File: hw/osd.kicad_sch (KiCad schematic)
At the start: 60 parts, among them U801 SN74CBTLV3125RGYR, U802 SN74CBTLV3125RGYR, U803 XLV320ADC5140IRTWR, U804 SN74CBTLV3125RGYR, U805 SN74CBTLV3125RGYR

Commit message: Now two CPLDs, new placement for better routing of clocks and symmetry for delay. Not routed yet but placement is "complete".
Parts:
- added R806, R807: 22, Resistor_SMD:R_0402_1005Metric, symbol Device:R_Small_US
- C817, C818, C830, C831, C836, C837, C842, C843: footprint Capacitor_SMD:C_0603_1608Metric -> Capacitor_SMD:C_0402_1005Metric
- U801, U802, U804, U805: footprint Library:RGY14_2P05X2P05 -> Library:DGV14; symbol Library:SN74CBTLV3125RGYR -> Library:SN74CBTLV3125
- renumbered C814 to C813, C815 to C814, C813 to C815, C841 to C840, C840 to C841, R806 to R808, R807 to R809, R808 to R810, R809 to R811, R810 to R812
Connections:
- net GND: no longer U801.15 (EPAD), U802.15 (EPAD), U804.15 (EPAD), U805.15 (EPAD)
- net osd.MISO: now also R806.1; no longer U803.15 (ADDR1_MISO)
- net osd.data: now also R807.1; no longer U803.21 (SDOUT)
- net swIn-: now reaches C845.2, R811.2, U804.12 (4A), U804.2 (1A), U804.5 (2A), U804.9 (3A), U805.12 (4A), U805.2 (1A), U805.5 (2A), U805.9 (3A)
- net swIn+: now reaches C822.2, R803.2, U801.12 (4A), U801.2 (1A), U801.5 (2A), U801.9 (3A), U802.12 (4A), U802.2 (1A), U802.5 (2A), U802.9 (3A)
- net osd.ph0 renamed osd.nPh0
- net osd.ph1 renamed osd.nPh1
- net osd.ph2 renamed osd.nPh2
- net osd.ph3 renamed osd.nPh3
- net osd.ph4 renamed osd.nPh4
- net osd.ph5 renamed osd.nPh5
- net osd.ph6 renamed osd.nPh6
- net osd.ph7 renamed osd.nPh7
- new net: R807.2, U803.21 (SDOUT)
- new net: R806.2, U803.15 (ADDR1_MISO)
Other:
- note added: "Length match the rf39-inner traces from switch to cap and route at 39 ohms."
- moved on the sheet: C802, C803, C804, C805, C806, C808, C809, C810, C812, C813, C814, C815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

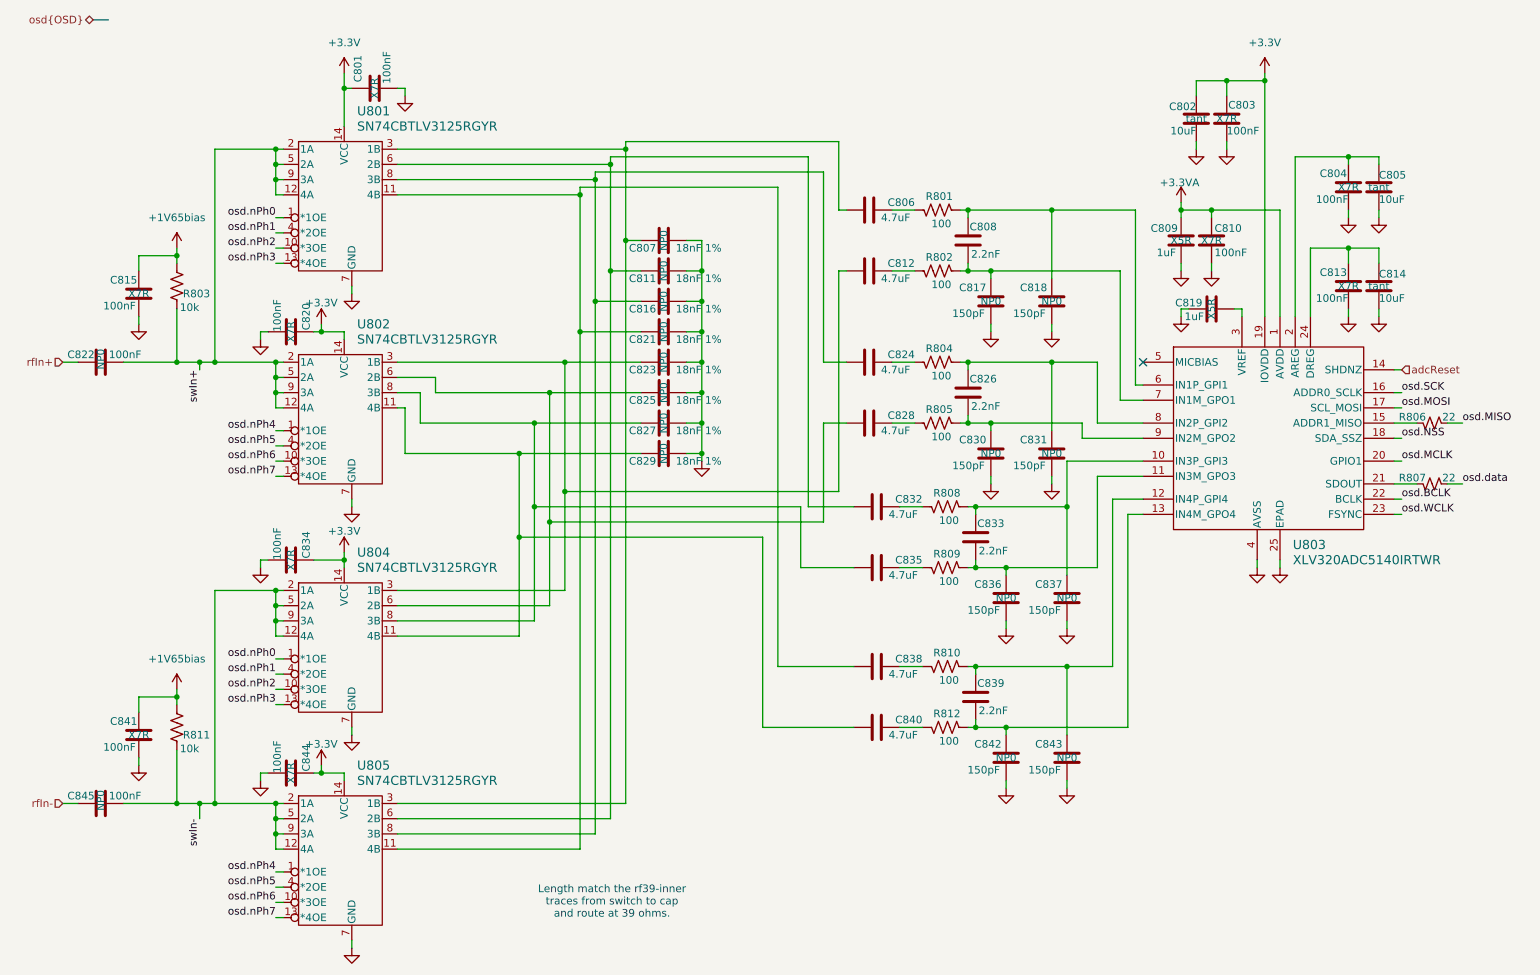
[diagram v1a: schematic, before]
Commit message: Checkpoint before replicating OSD and then CPLD layout from 0 to 1
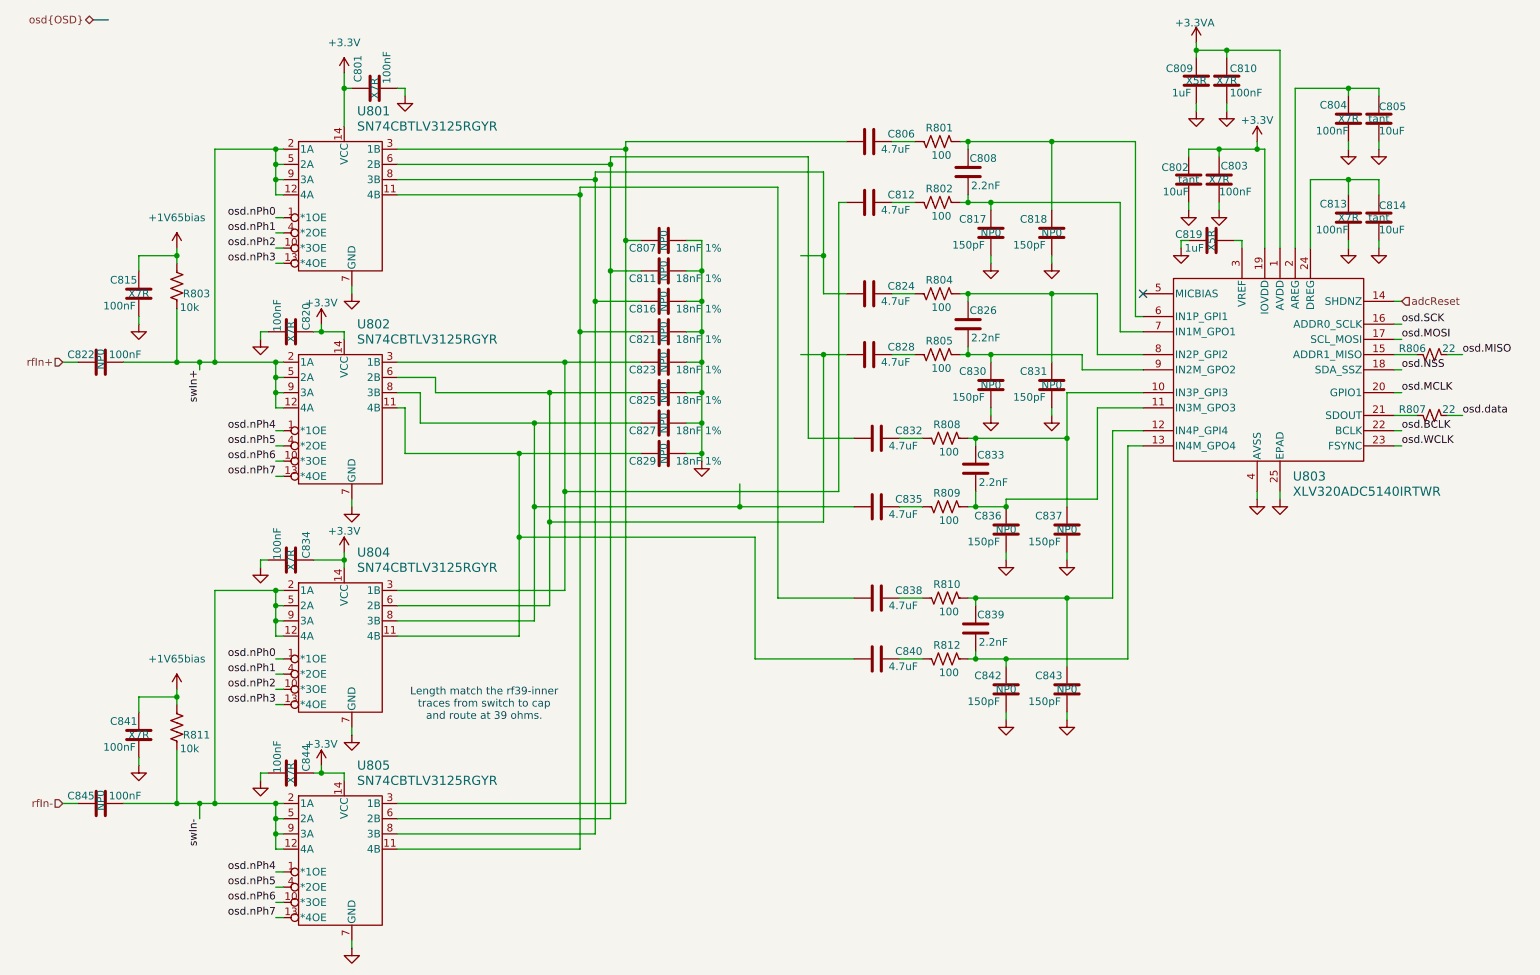
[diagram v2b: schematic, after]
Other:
- moved on the sheet: C802, C803, C804, C805, C806, C808, C809, C810, C812, C813, C814, C817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

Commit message: CPLDs and OSDs routed?
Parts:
- renumbered C809 to C801, C810 to C802, C801 to C803, C808 to C807, C802 to C808, C803 to C809, C812 to C810, C813 to C811, C814 to C812, C817 to C813, C818 to C814, C807 to C815, C819 to C816, C811 to C817, C815 to C818, C824 to C819, C816 to C820, C826 to C821, C820 to C822, C821 to C823, C828 to C824, C822 to C825, C823 to C826, C830 to C827, C831 to C828, C825 to C829, C827 to C830, C832 to C831, C829 to C832, C835 to C834, C836 to C835, C837 to C836, C834 to C837, C842 to C841, C843 to C842, C841 to C843, R812 to R811, R811 to R812, U803 to U802, U802 to U803

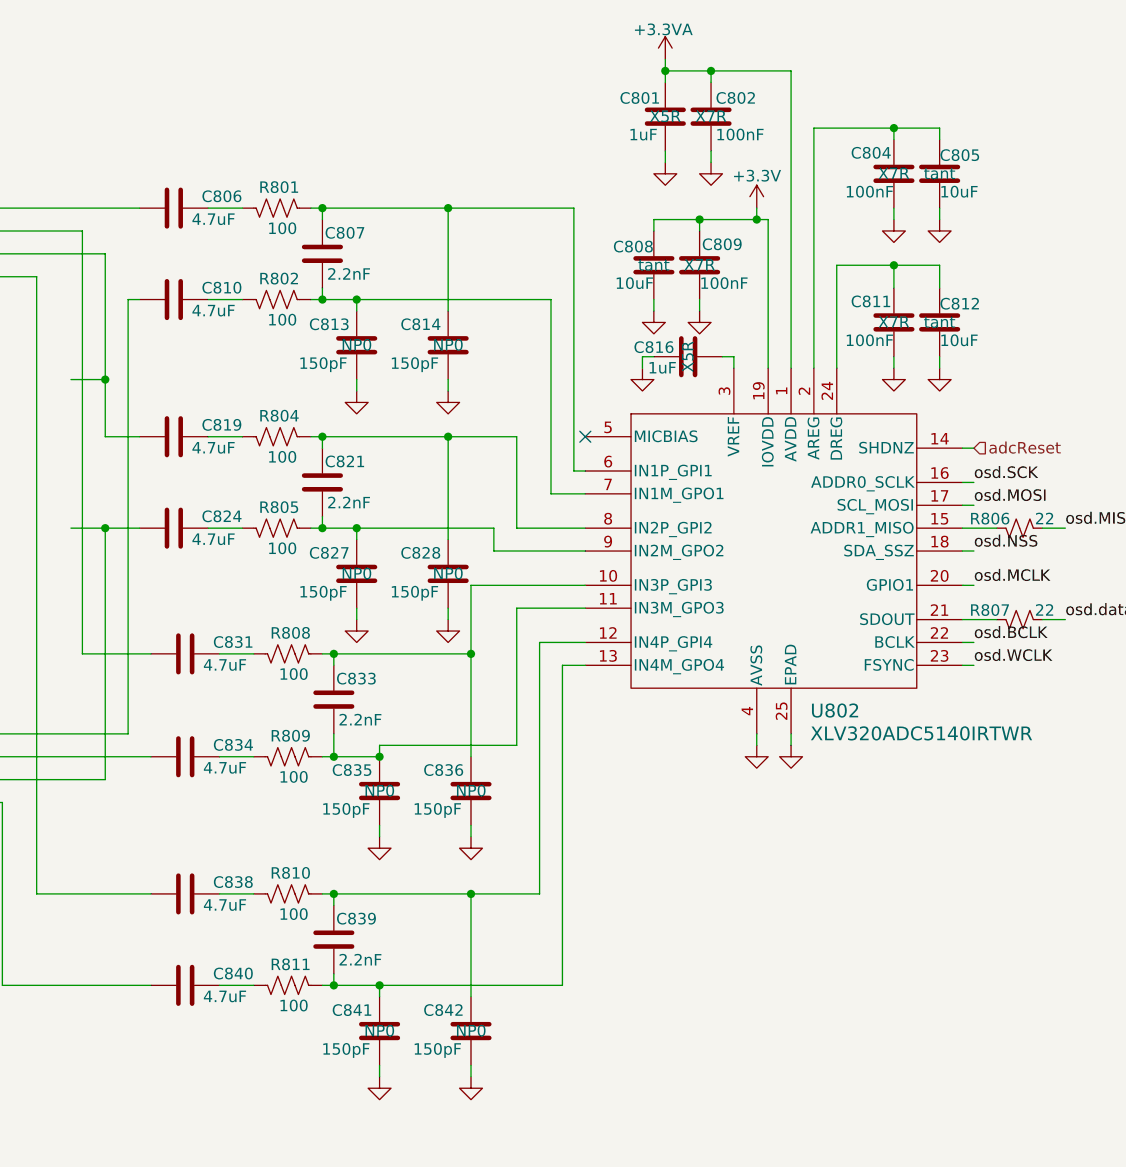
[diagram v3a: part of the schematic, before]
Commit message: 3D rendering now. All DRCs pass on schematic and PCB. BOM scrubbed to coallesce parts. Still no part numbers for most.
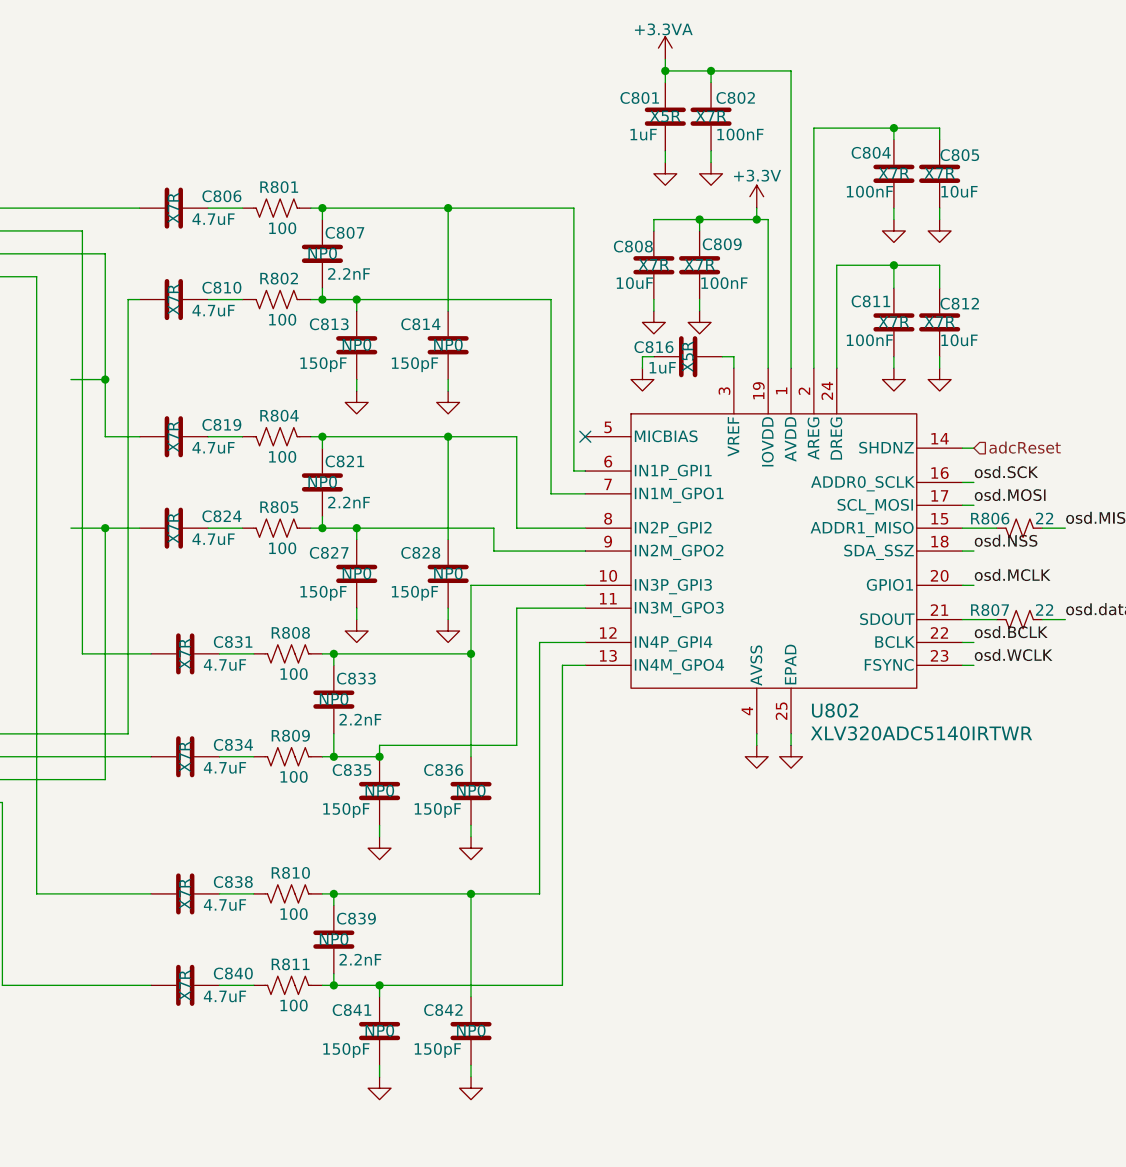
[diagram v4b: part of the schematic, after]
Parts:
- C805, C808, C812: footprint Capacitor_SMD:C_0805_2012Metric -> Capacitor_SMD:C_0603_1608Metric; cap-type tant -> X7R; working-voltage 10V -> 25V
- C806, C810, C819, C824, C831, C834, C838, C840: cap-type (none) -> X7R
- C807, C821, C833, C839: cap-type (none) -> NP0; working-voltage 50V -> 25V
- C813, C814, C827, C828, C835, C836, C841, C842: working-voltage 50V -> 25V
- C825, C845: working-voltage 50V -> 100V
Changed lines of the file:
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@@
 			)
 		)
-		(property "working-voltage" "50V"
+		(property "working-voltage" "100V"
 			(at 26.67 148.59 0)
 			(effects
@@
 			)
 		)
-		(property "cap-type" ""
+		(property "cap-type" "NP0"
 			(at 172.72 119.38 0)
 			(effects
@@
 			)
 		)
-		(property "working-voltage" "50V"
+		(property "working-voltage" "25V"
 			(at 172.72 119.38 0)
 			(effects
@@
 			)
 		)
-		(property "Footprint" "Capacitor_SMD:C_0805_2012Metric"
+		(property "Footprint" "Capacitor_SMD:C_0603_1608Metric"
 			(at 240.9952 54.61 0)
 			(effects
@@
 			)
 		)
-		(property "cap-type" "tant"
+		(property "cap-type" "X7R"
 			(at 240.03 50.8 0)
 			(effects
@@
 			)
 		)
-		(property "working-voltage" "10V"
+		(property "working-voltage" "25V"
 			(at 240.03 50.8 0)
 			(effects
@@
 			)
 		)
-		(property "cap-type" ""
+		(property "cap-type" "X7R"
 			(at 156.21 114.3 0)
 			(effects
@@
 			)
 		)
-		(property "cap-type" ""
+		(property "cap-type" "NP0"
 			(at 172.72 92.71 0)
 			(effects
@@
 			)
 		)
-		(property "working-voltage" "50V"
+		(property "working-voltage" "25V"
 			(at 172.72 92.71 0)
 			(effects
@@
 			)
 		)
-		(property "working-voltage" "50V"
+		(property "working-voltage" "25V"
 			(at 177.8 129.54 0)
 			(effects
@@
 			)
 		)
-		(property "cap-type" ""
+		(property "cap-type" "X7R"
 			(at 156.21 99.06 0)
 			(effects
@@
 			)
 		)
-		(property "working-voltage" "50V"
+		(property "working-voltage" "25V"
 			(at 185.42 78.74 0)
 			(effects
@@
 			)
 		)
-		(property "cap-type" ""
+		(property "cap-type" "NP0"
 			(at 171.45 43.18 0)
 			(effects
@@
 			)
 		)
-		(property "working-voltage" "50V"
+		(property "working-voltage" "25V"
 			(at 171.45 43.18 0)
 			(effects
@@
 			)
 		)
-		(property "working-voltage" "50V"
+		(property "working-voltage" "25V"
 			(at 175.26 78.74 0)
 			(effects
@@
 			)
 		)
-		(property "cap-type" ""
+		(property "cap-type" "X7R"
 			(at 154.94 73.66 0)
 			(effects
@@
 			)
 		)
-		(property "Footprint" "Capacitor_SMD:C_0805_2012Metric"
+		(property "Footprint" "Capacitor_SMD:C_0603_1608Metric"
 			(at 240.9952 38.1 0)
 			(effects
@@
 			)
 		)
-		(property "cap-type" "tant"
+		(property "cap-type" "X7R"
 			(at 240.03 34.29 0)
 			(effects
@@
 			)
 		)
-		(property "working-voltage" "10V"
+		(property "working-voltage" "25V"
 			(at 240.03 34.29 0)
 			(effects
@@
 			)
 		)
-		(property "cap-type" ""
+		(property "cap-type" "X7R"
 			(at 156.21 124.46 0)
 			(effects
@@
 			)
 		)
-		(property "cap-type" ""
+		(property "cap-type" "X7R"
 			(at 154.94 63.5 0)
 			(effects
@@
 			)
 		)
-		(property "working-voltage" "50V"
+		(property "working-voltage" "25V"
 			(at 187.96 129.54 0)
 			(effects
@@
 			)
 		)
-		(property "working-voltage" "50V"
+		(property "working-voltage" "25V"
 			(at 177.8 102.87 0)
 			(effects
@@
 			)
 		)
-		(property "Footprint" "Capacitor_SMD:C_0805_2012Metric"
+		(property "Footprint" "Capacitor_SMD:C_0603_1608Metric"
 			(at 207.3148 48.26 0)
 			(effects
@@
 			)
 		)
-		(property "cap-type" "tant"
+		(property "cap-type" "X7R"
 			(at 208.28 44.45 0)
 			(effects
@@
 			)
 		)
-		(property "working-voltage" "10V"
+		(property "working-voltage" "25V"
 			(at 208.28 44.45 0)
 			(effects
@@
 			)
 		)
-		(property "working-voltage" "50V"
+		(property "working-voltage" "25V"
 			(at 187.96 102.87 0)
 			(effects
@@
 			)
 		)
-		(property "cap-type" ""
+		(property "cap-type" "X7R"
 			(at 154.94 38.1 0)
 			(effects
@@
 			)
 		)
-		(property "working-voltage" "50V"
+		(property "working-voltage" "25V"
 			(at 185.42 53.34 0)
 			(effects
@@
 			)
 		)
-		(property "working-voltage" "50V"
+		(property "working-voltage" "100V"
 			(at 26.67 74.93 0)
 			(effects
@@
 			)
 		)
-		(property "cap-type" ""
+		(property "cap-type" "NP0"
 			(at 171.45 68.58 0)
 			(effects
@@
 			)
 		)
-		(property "working-voltage" "50V"
+		(property "working-voltage" "25V"
 			(at 171.45 68.58 0)
 			(effects
@@
 			)
 		)
-		(property "cap-type" ""
+		(property "cap-type" "X7R"
 			(at 154.94 48.26 0)
 			(effects
@@
 			)
 		)
-		(property "working-voltage" "50V"
+		(property "working-voltage" "25V"
 			(at 175.26 53.34 0)
 			(effects
@@
 			)
 		)
-		(property "cap-type" ""
+		(property "cap-type" "X7R"
 			(at 156.21 87.63 0)
 			(effects
